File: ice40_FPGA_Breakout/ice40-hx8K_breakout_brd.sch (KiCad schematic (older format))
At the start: 13 parts

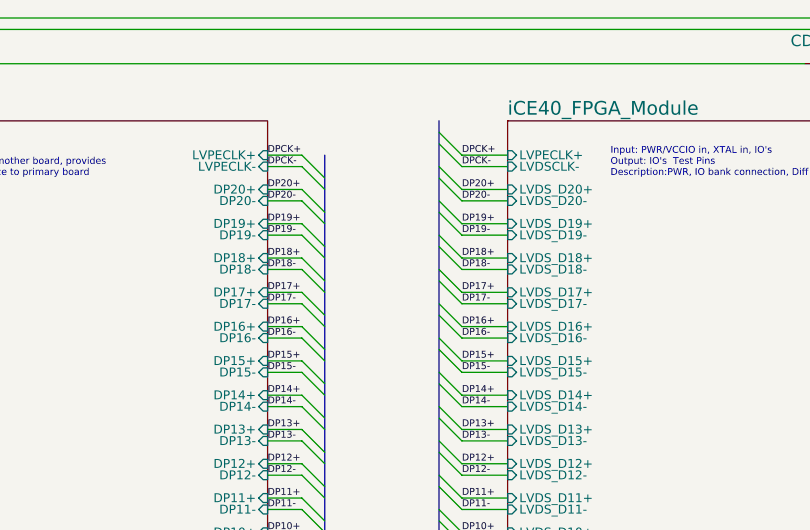
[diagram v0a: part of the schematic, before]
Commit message: update differential pair connection in schematic and updating layout placement for diff pair
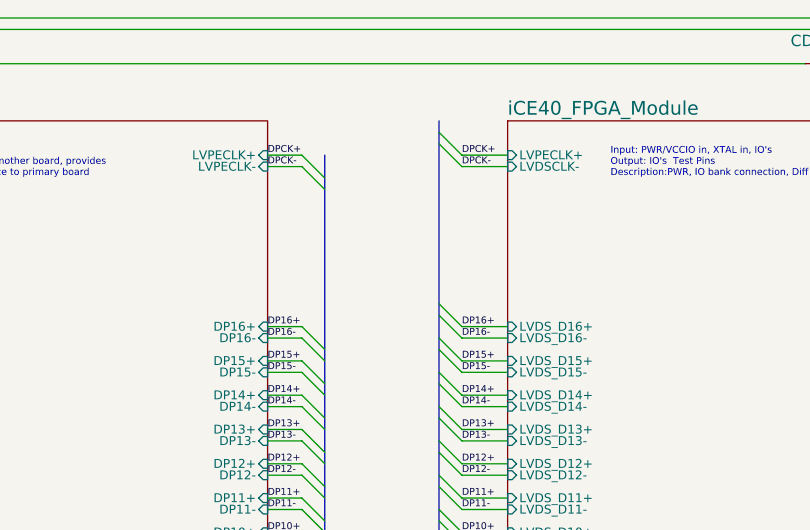
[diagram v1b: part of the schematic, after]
